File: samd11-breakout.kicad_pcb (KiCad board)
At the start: 2 copper layers, 38.4 x 25.9 mm, 17 parts, among them J1 USB_C_Receptacle, J2 DebugEdge_02x03, J3 Conn_01x10_Male, J4 Conn_01x10_Male, U1 USBLC6-2SC6, U2 MCP1700-3302E_SOT23, U3 SAMD11D14A-M

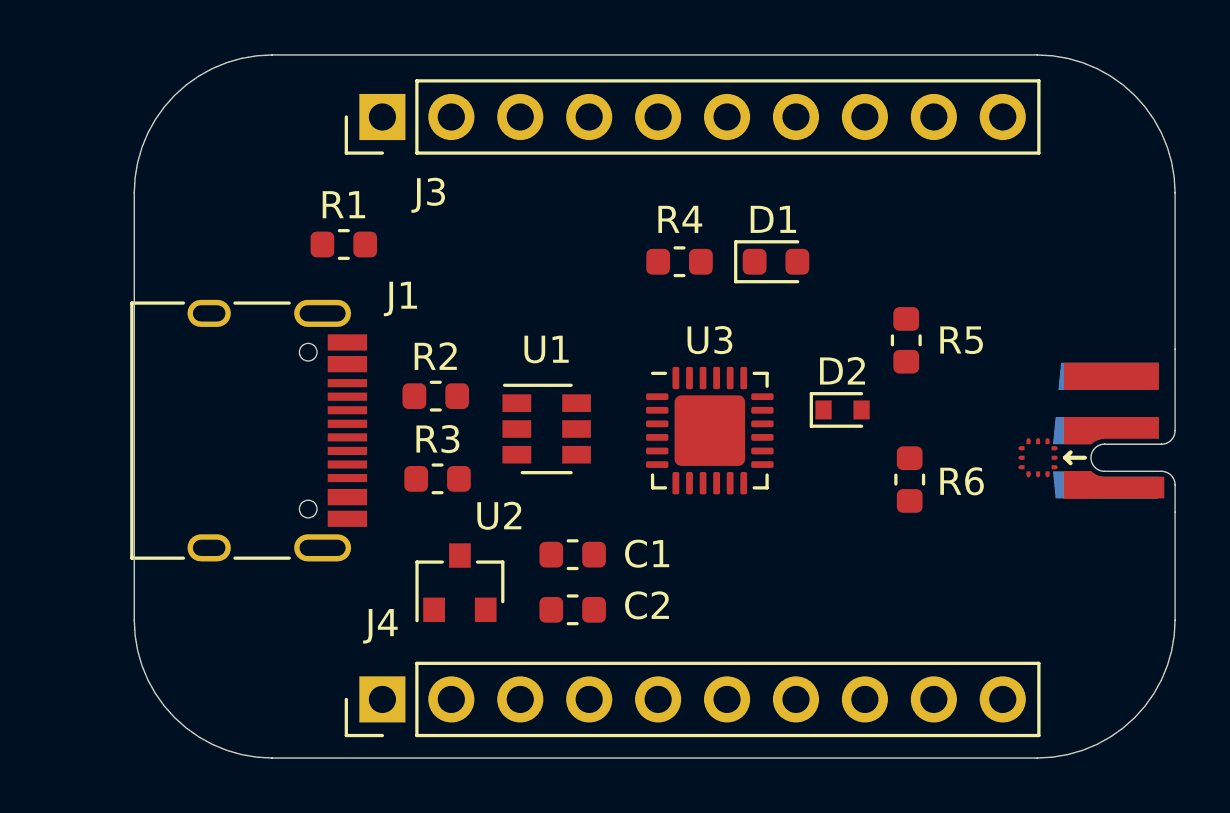
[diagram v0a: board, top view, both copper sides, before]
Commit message: half routed
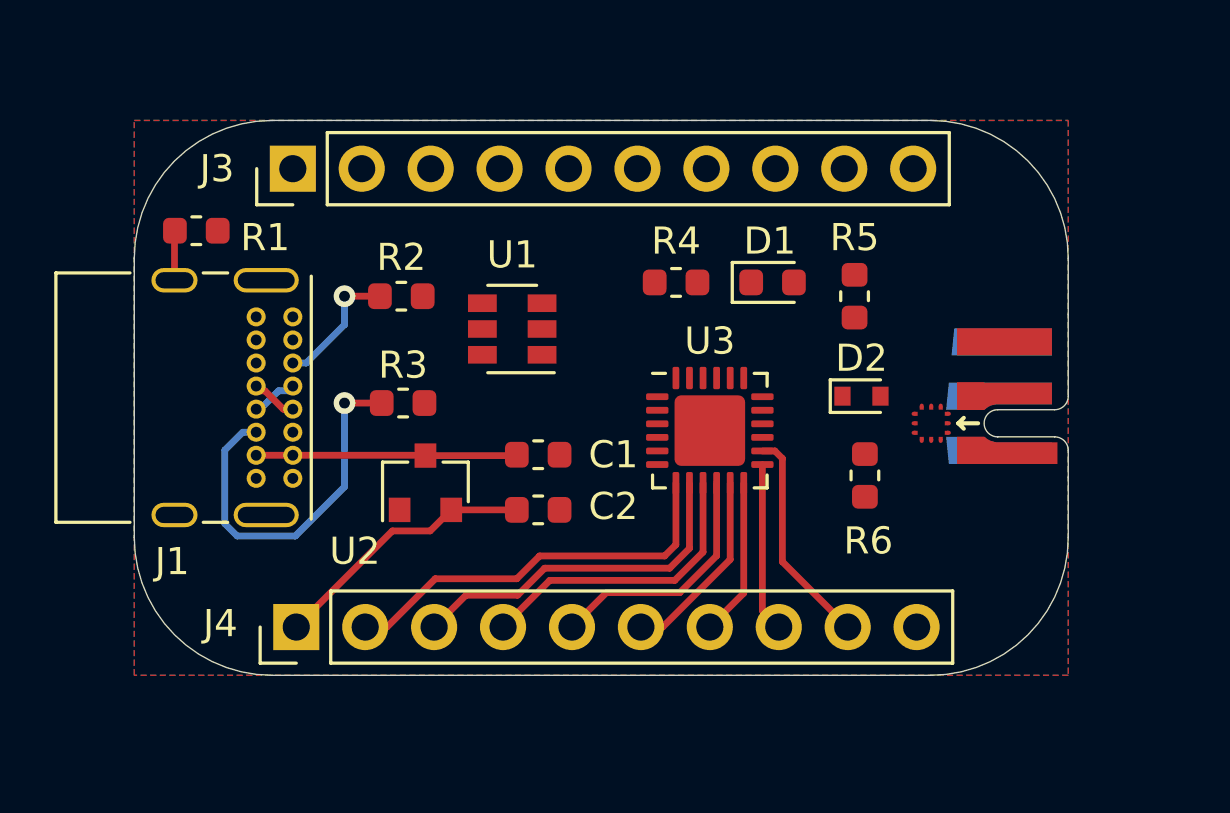
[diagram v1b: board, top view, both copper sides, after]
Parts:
- J1: footprint project:USB_C_Receptacle_HRO_TYPE-C-31-M-12 -> project:USB_C_Receptacle_GCT_USB4085
- moved R1 5.46 mm to (112.4, 73.3)
- moved J1 4.66 mm to (116.0, 76.5)
- moved J4 4.15 mm to (116.1, 87.9)
- moved J2 4.14 mm to (144.5, 79.4)
- moved R2 3.90 mm to (119.9, 75.7)
- moved U1 3.90 mm to (124.0, 76.9), turned to 180 degrees
- moved U2 3.90 mm to (120.8, 82.6)
- moved C1 3.90 mm to (125.0, 81.5)
- moved C2 3.90 mm to (125.0, 83.6)
- moved J3 3.81 mm to (116.0, 71.0)
- moved R3 3.07 mm to (120.0, 79.6), turned to 180 degrees
- moved R5 2.50 mm to (136.7, 75.7)
- moved R6 1.66 mm to (137.0, 82.3)
- moved D2 0.86 mm to (136.9, 79.4)
- moved R4 0.77 mm to (130.1, 75.2)
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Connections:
- net /USB_DM renamed /USB_D-
- net /USB_DP renamed /USB_D+
- J3 pad 2: /PA02 -> /PA07
- J3 pad 3: /PA03 -> /PA06
- J3 pad 4: /PA04 -> /PA05
- J3 pad 5: /PA05 -> /PA04
- J3 pad 6: /PA06 -> /PA03
- J3 pad 7: /PA07 -> /PA02
- J3 pad 8: /PA08 -> /PA23
- J3 pad 9: /PA09 -> /PA22
- J4 pad 2: /PA10 -> /PA08
- J4 pad 3: /PA11 -> /PA09
- J4 pad 4: /PA14 -> /PA10
- J4 pad 5: /PA15 -> /PA11
- J4 pad 6: /PA16 -> /PA14
- J4 pad 7: /PA17 -> /PA15
- J4 pad 8: /PA22 -> /PA16
- J4 pad 9: /PA23 -> /PA17
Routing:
- net /PA08: track 0.00 -> 15.0 mm
- net Net-(J1-PadB5): track 0.00 -> 13.9 mm, vias 0 -> 1
- net /PA09: track 0.00 -> 13.0 mm
- net /PA10: track 0.00 -> 11.1 mm
- net +3V3: track 0.00 -> 9.92 mm
- net +5V: track 0.00 -> 9.62 mm
- net /PA11: track 0.00 -> 9.09 mm
- net /PA17: track 0.00 -> 8.06 mm
- net /PA14: track 0.00 -> 7.13 mm
- net /PA16: track 0.00 -> 6.24 mm
- net /PA15: track 0.00 -> 5.82 mm
- net Net-(J1-PadA5): track 0.00 -> 4.85 mm, vias 0 -> 1
- net Net-(J1-PadS1): track 0.00 -> 1.83 mm
- net /USB_D-: track 0.00 -> 1.80 mm
- net /USB_D+: track 0.00 -> 1.77 mm
- added copper zone on B.Cu, net GND
- added copper zone on F.Cu, net GND
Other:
- board size 38.4 x 25.9 mm -> 34.4 x 20.4 mm

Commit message: ok that should do it
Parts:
- J1: value USB_C_Receptacle -> USB4105-GF-A; footprint project:USB_C_Receptacle_GCT_USB4085 -> project:GCT_USB4105-GF-A
- moved J1 5.11 mm to (111.8, 79.4)
- moved R2 3.96 mm to (120.4, 79.6)
- moved R3 3.96 mm to (120.4, 75.7)
- moved J4 0.25 mm to (116.1, 87.6)
- moved J3 0.13 mm to (116.0, 71.1)
- turned U1 to 0 degrees
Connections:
- J1 pad A5: Net-(J1-PadA5) -> /CC1
- J1 pad A8: Net-(J1-PadA8) -> /USB_SHIELD
- J1 pad B5: Net-(J1-PadB5) -> /CC2
- J1 pad B6: /USB_D+ -> /USB_D-
- J1 pad B7: /USB_D- -> /USB_D+
- J1 pad B8: Net-(J1-PadB8) -> /USB_SHIELD
- J1 pad S1: Net-(J1-PadS1) -> /USB_SHIELD
- J3 pad 8: /PA23 -> /PA27
- J3 pad 9: /PA22 -> /PA23
- R1 pad 1: Net-(J1-PadS1) -> /USB_SHIELD
- R2 pad 1: Net-(J1-PadA5) -> /CC2
- R3 pad 2: Net-(J1-PadB5) -> /CC1
- U3 pad 15: /PA22 -> /VBUS_SENSE
- U3 pad 17: /VBUS_SENSE -> /PA27
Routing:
- net +3V3: track 9.92 -> 55.2 mm, vias 0 -> 2
- net +5V: track 9.62 -> 40.9 mm, vias 0 -> 2
- net /USB_SHIELD: track 0.00 -> 27.0 mm, vias 0 -> 2
- net /USB_D+: track 1.77 -> 19.5 mm, vias 0 -> 2
- net /PA07: track 0.00 -> 17.5 mm
- net /USB_D-: track 1.80 -> 18.8 mm, vias 0 -> 2
- net /PA06: track 0.00 -> 14.7 mm
- net Net-(J1-PadB5): track 13.9 -> 0.00 mm, vias 1 -> 0
- net /PA05: track 0.00 -> 12.6 mm
- net /SWDCLK: track 0.00 -> 12.5 mm, vias 0 -> 1
- net /PA02: track 0.00 -> 12.4 mm
- net /PA23: track 0.00 -> 11.8 mm, vias 0 -> 1
- net /PA04: track 0.00 -> 11.3 mm
- net /PA27: track 0.00 -> 10.7 mm, vias 0 -> 1
- net /PA03: track 0.00 -> 10.5 mm
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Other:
- net class Default: clearance 0.2 -> 0.1524; trace_width 0.25 -> 0.1524; via_dia 0.8 -> 0.6858; via_drill 0.4 -> 0.3302
- net class Power added: clearance 0.1524, trace_width 0.25, via_dia 0.6858, via_drill 0.3302
- rule pad_to_mask_clearance: 0 -> 0.000051
- rule trace_clearance: 0.2 -> 0.1524
- rule trace_min: 0.2 -> 0.1524
- rule via_min_drill: 0.3 -> 0.254
- rule via_min_size: 0.4 -> 0.508

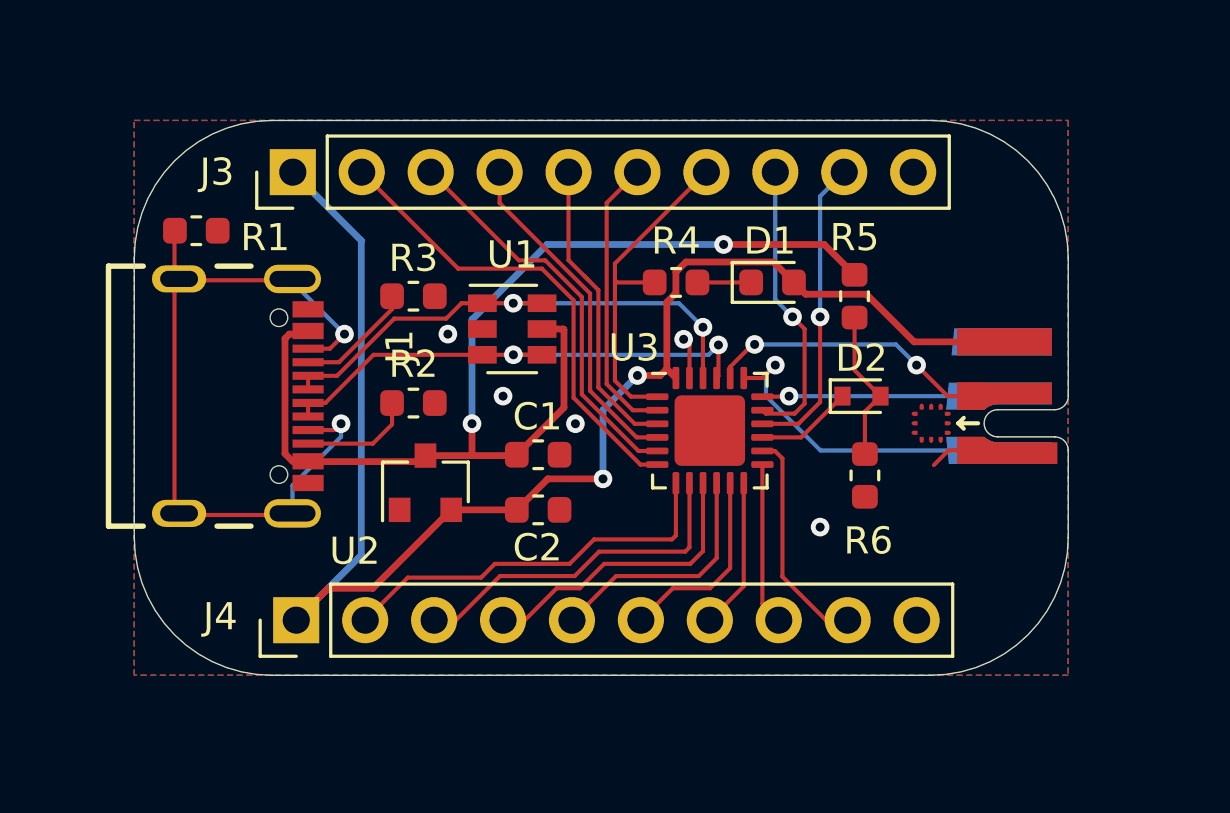
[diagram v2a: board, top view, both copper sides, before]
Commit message: add silk text to back
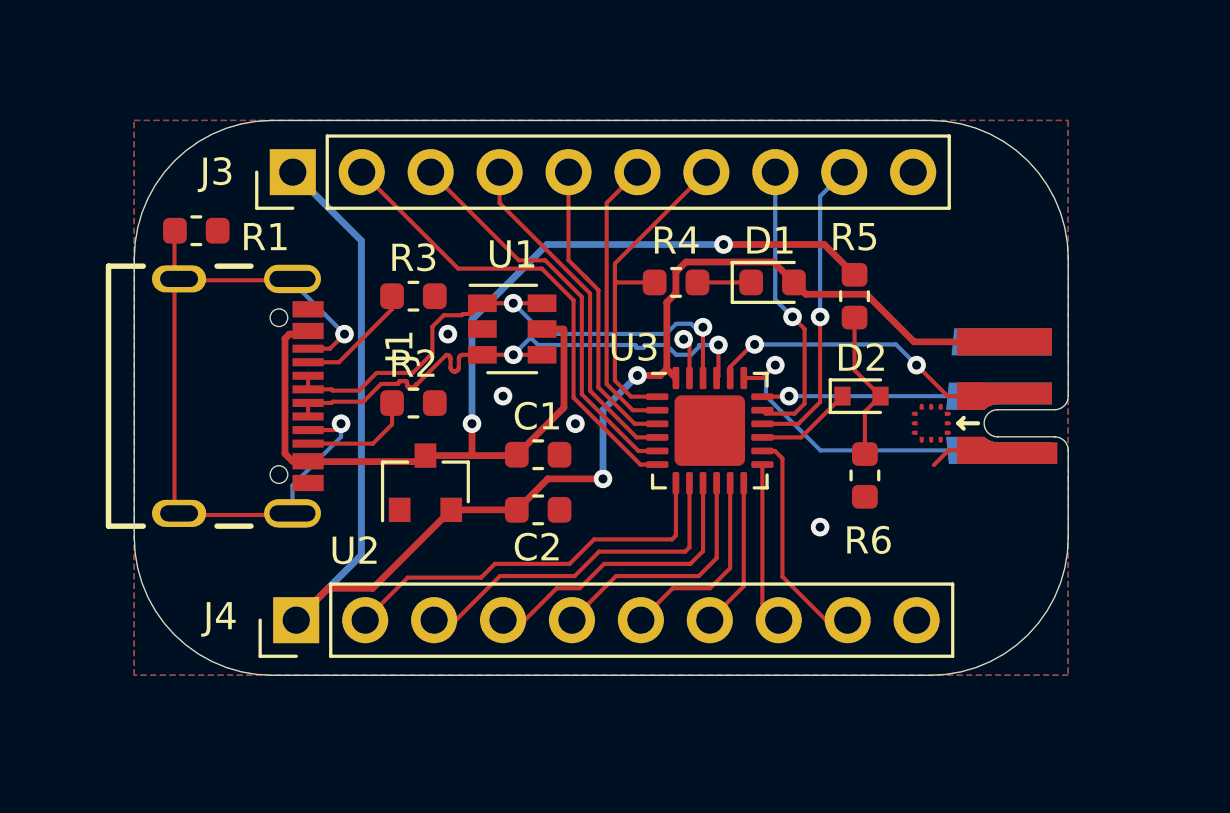
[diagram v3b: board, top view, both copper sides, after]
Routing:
- net /USB_D-: track 18.8 -> 20.8 mm
- net /USB_D+: track 19.5 -> 21.0 mm
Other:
- board text added: "+3 P07 P06 p05 P04 P03 P02 P27 P23 GND"
- board text added: "+3 P08 P09 P10 P11 P14 P15 P16 P17 GND"
- board text added: "github.com/noahp/ samd11-breakout v1"
